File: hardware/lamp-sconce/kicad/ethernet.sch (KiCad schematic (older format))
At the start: 27 parts

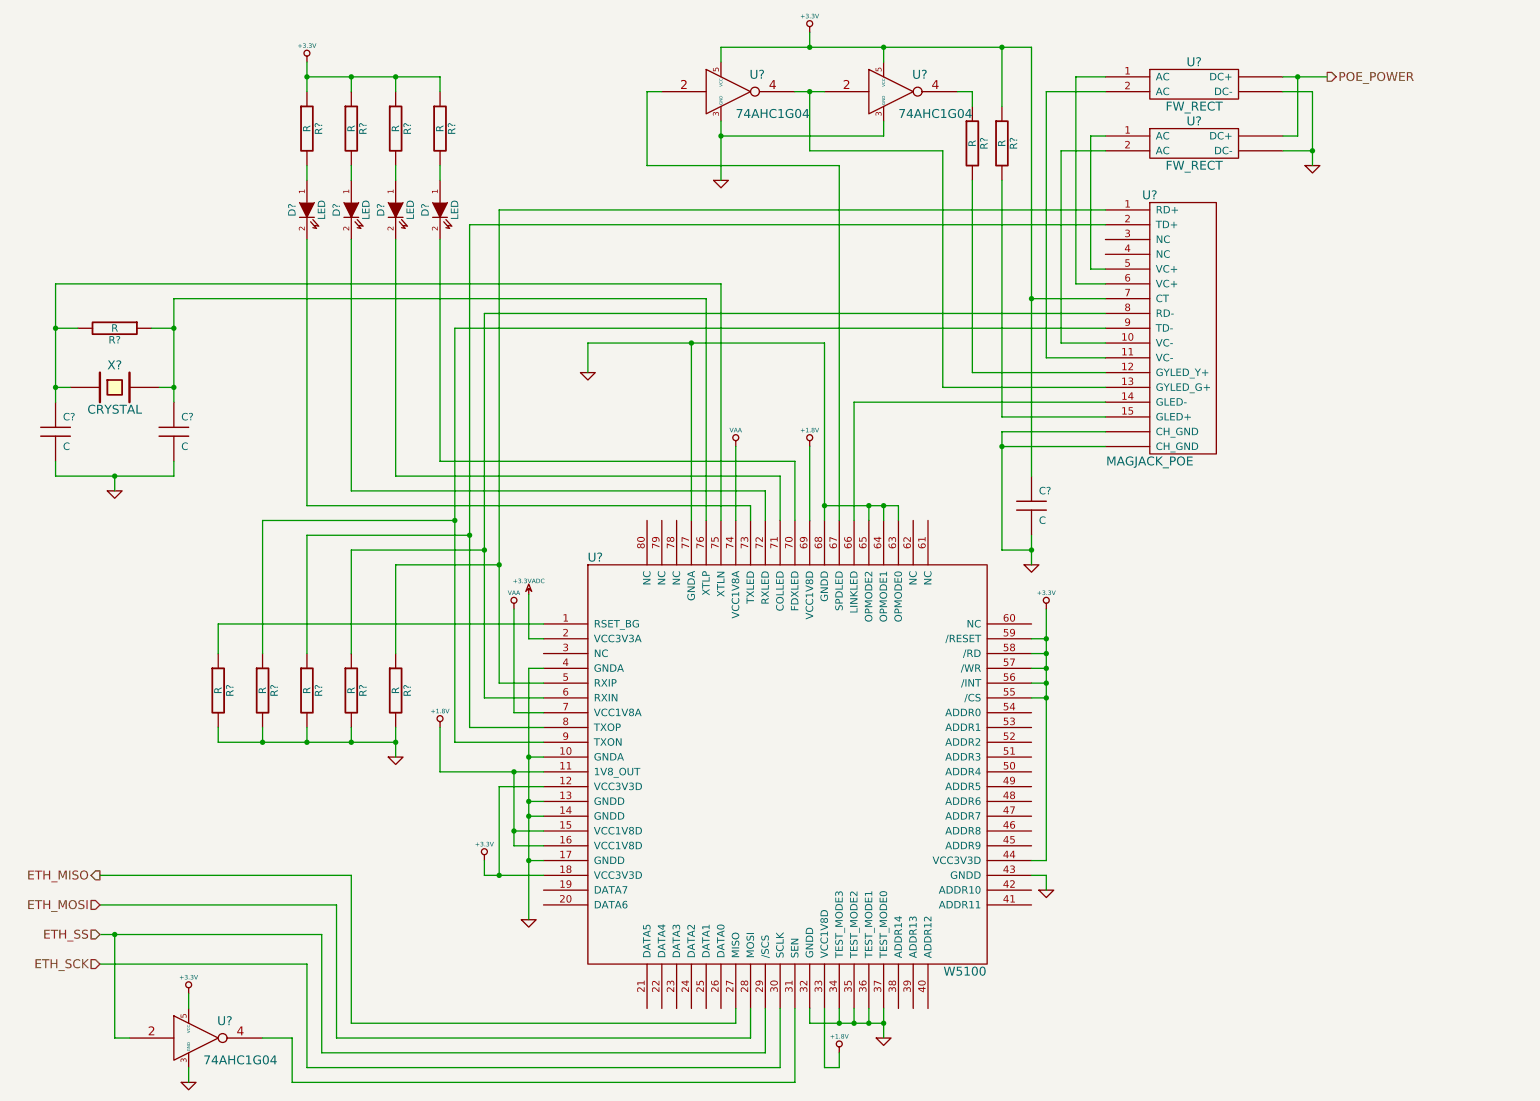
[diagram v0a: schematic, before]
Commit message: Adding more work for the sconce lamp.  Schematic is pretty much complete.
Signed-off-by: Daniel P Williams <dwilliams@port8080.net>
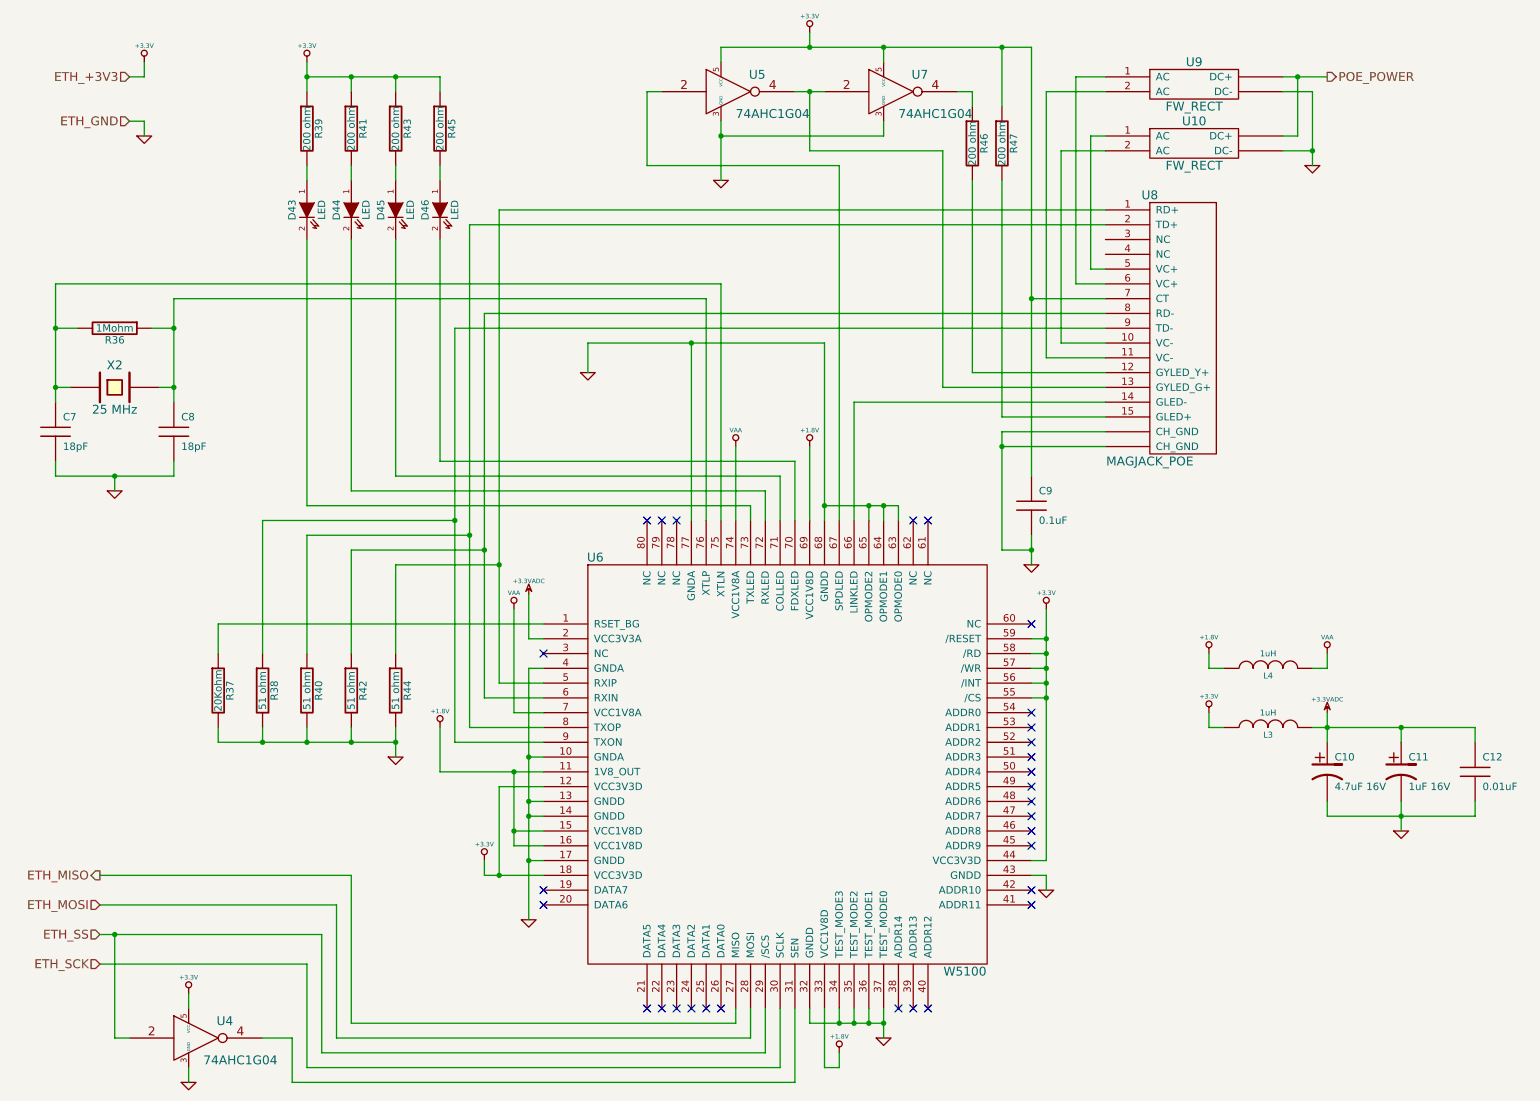
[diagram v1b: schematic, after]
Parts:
- added C10: 4.7uF 16V, symbol CP1
- added C11: 1uF 16V, symbol CP1
- added C12: 0.01uF, symbol C
- added L3, L4: 1uH, symbol INDUCTOR
- C7, C8: renamed from C?; value C -> 18pF
- C9: renamed from C?; value C -> 0.1uF
- R36: renamed from R?; value R -> 1Mohm
- R37: renamed from R?; value R -> 20Kohm
- R38, R40, R42, R44: renamed from R?; value R -> 51 ohm
- R39, R41, R43, R45, R46, R47: renamed from R?; value R -> 200 ohm
- X2: renamed from X?; value CRYSTAL -> 25 MHz
- gave numbers to parts that had none: 11
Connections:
- net +1.8V: now also L4.1
- net +3.3V: now also L3.1
- net +3.3VADC: now also C10.1, C11.1, C12.1, L3.2
- net GND: now also C10.2, C11.2, C12.2
- net VAA: now also L4.2
- no-connect marks 0 -> 30
